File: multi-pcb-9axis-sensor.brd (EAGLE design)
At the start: 26.7 x 26.7 mm, 2 parts, among them X1 2.54B-ZR

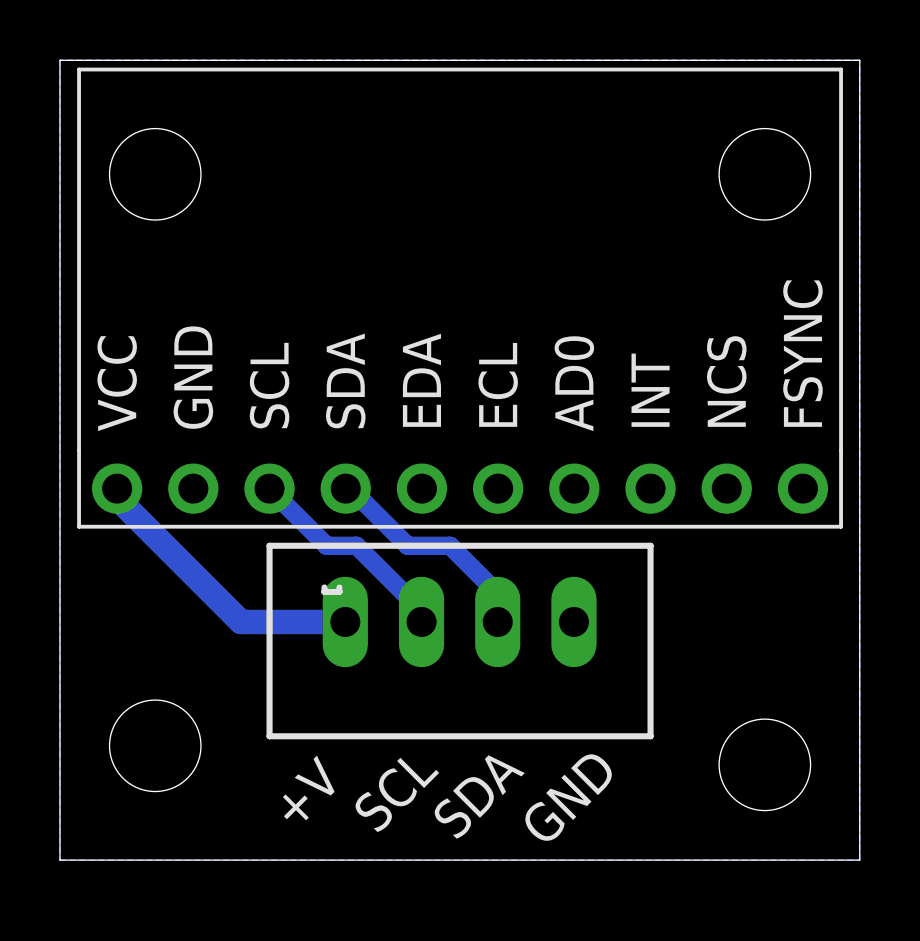
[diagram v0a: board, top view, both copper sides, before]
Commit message: Routed more multi-pcb boards
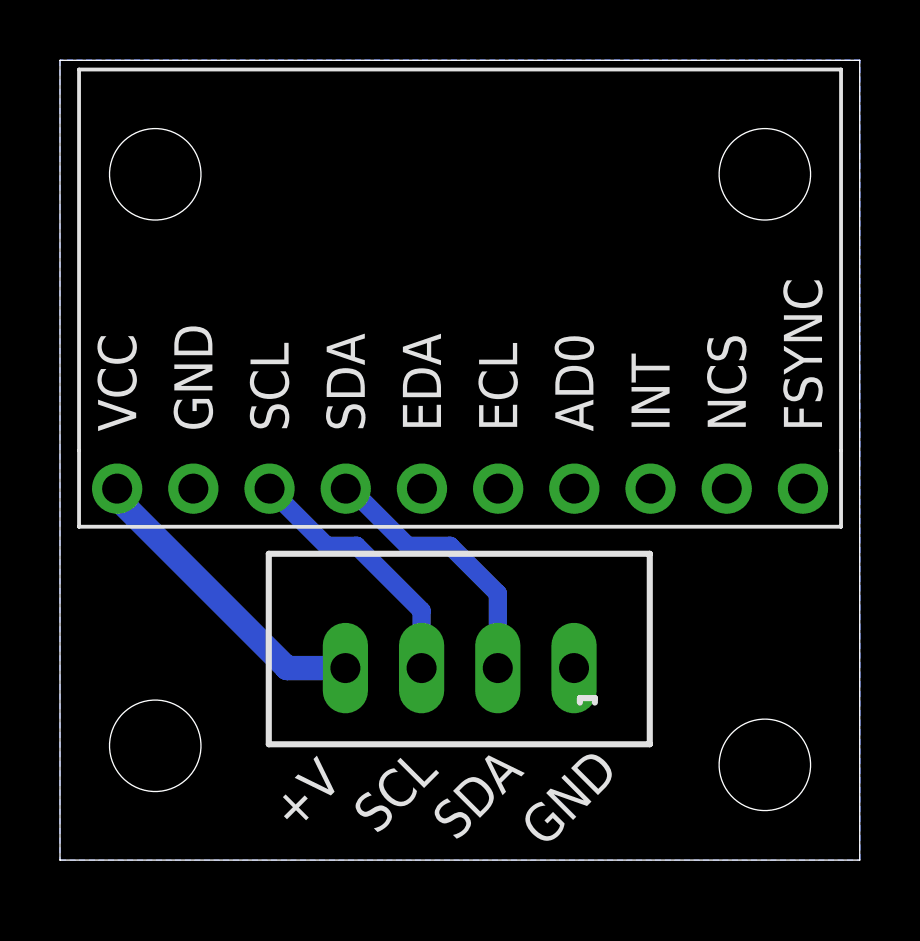
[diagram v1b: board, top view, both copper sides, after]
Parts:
- moved X1 1.54 mm to (13.3, 6.40), turned to 180 degrees
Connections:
- net +3V3: now also X1.4; no longer X1.1
- net GND: now also X1.1; no longer X1.4
- net I2C0_SCL: now also X1.3; no longer X1.2
- net I2C0_SDA: now also X1.2; no longer X1.3
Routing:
- net I2C0_SDA: track 7.47 -> 9.00 mm
- net I2C0_SCL: track 7.13 -> 8.66 mm
- net +3V3: track 9.63 -> 10.3 mm
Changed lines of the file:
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@@
 <elements>
 <element name="U$3" library="MPU9250" package="MPU9250_BREAKOUT" value="MPU9250_BREAKOUT" x="13.335" y="18.7325" smashed="yes" rot="R90"/>
-<element name="X1" library="con-jst-custom" package="B4B-ZR2.5" value="2.54B-ZR" x="13.335" y="7.9375" smashed="yes"/>
+<element name="X1" library="con-jst-custom" package="B4B-ZR2.5" value="2.54B-ZR" x="13.3096" y="6.4008" smashed="yes" rot="R180">
+<attribute name="VALUE" x="18.3296" y="12.4408" size="1.27" layer="27" rot="R180"/>
+</element>
 </elements>
 <signals>
 <signal name="+3V3">
 <contactref element="U$3" pad="VCC"/>
-<contactref element="X1" pad="1"/>
-<wire x1="6.0325" y1="7.9375" x2="1.905" y2="12.065" width="0.8128" layer="16"/>
 <wire x1="1.905" y1="12.3825" x2="1.905" y2="12.065" width="0.8128" layer="16"/>
-<wire x1="6.0325" y1="7.9375" x2="9.5102" y2="7.9375" width="0.8128" layer="16"/>
+<contactref element="X1" pad="4"/>
+<wire x1="7.5692" y1="6.4008" x2="9.513" y2="6.4008" width="0.8128" layer="16"/>
+<wire x1="1.905" y1="12.065" x2="7.5692" y2="6.4008" width="0.8128" layer="16"/>
 </signal>
 <signal name="GND">
 <contactref element="U$3" pad="GND"/>
 <contactref element="U$3" pad="FSYNC"/>
-<contactref element="X1" pad="4"/>
 <polygon width="0.4064" layer="16" spacing="0.0254">
 <vertex x="0" y="26.67"/>
@@
 <vertex x="26.67" y="26.67"/>
 </polygon>
+<contactref element="X1" pad="1"/>
 </signal>
 <signal name="I2C0_SDA">
 <contactref element="U$3" pad="SDA"/>
-<contactref element="X1" pad="3"/>
-<wire x1="14.5916" y1="7.9375" x2="14.5916" y2="8.89" width="0.6096" layer="16"/>
-<wire x1="14.5916" y1="8.89" x2="13.0041" y2="10.4775" width="0.6096" layer="16"/>
-<wire x1="13.0041" y1="10.4775" x2="11.58875" y2="10.4775" width="0.6096" layer="16"/>
+<wire x1="11.58875" y1="10.4775" x2="13.0041" y2="10.4775" width="0.6096" layer="16"/>
 <wire x1="11.58875" y1="10.4775" x2="9.68375" y2="12.3825" width="0.6096" layer="16"/>
 <wire x1="9.68375" y1="12.3825" x2="9.525" y2="12.3825" width="0.6096" layer="16"/>
+<contactref element="X1" pad="2"/>
+<wire x1="14.593" y1="8.8886" x2="14.593" y2="6.4008" width="0.6096" layer="16"/>
+<wire x1="13.0041" y1="10.4775" x2="14.593" y2="8.8886" width="0.6096" layer="16"/>
 </signal>
 <signal name="I2C0_SCL">
 <contactref element="U$3" pad="SCL"/>
-<contactref element="X1" pad="2"/>
-<wire x1="12.0516" y1="7.9375" x2="12.0516" y2="8.31215" width="0.6096" layer="16"/>
-<wire x1="12.0516" y1="8.31215" x2="9.88625" y2="10.4775" width="0.6096" layer="16"/>
-<wire x1="9.88625" y1="10.4775" x2="8.89" y2="10.4775" width="0.6096" layer="16"/>
+<wire x1="8.89" y1="10.4775" x2="9.88625" y2="10.4775" width="0.6096" layer="16"/>
 <wire x1="8.89" y1="10.4775" x2="6.985" y2="12.3825" width="0.6096" layer="16"/>
+<contactref element="X1" pad="3"/>
+<wire x1="12.053" y1="8.31075" x2="12.053" y2="6.4008" width="0.6096" layer="16"/>
+<wire x1="9.88625" y1="10.4775" x2="12.053" y2="8.31075" width="0.6096" layer="16"/>
 </signal>
 </signals>
